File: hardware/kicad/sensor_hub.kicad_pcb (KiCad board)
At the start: 2 copper layers, 0 parts

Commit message: hardware: first board placement, outline and 230 VAC design rules
- Board 100 x 100 mm (fits 8 mm MAINS separation + socketed Pico WH),
  4x M3 holes (board-only), 2 mm isolation slots: under the relays
  (coil | contacts) and along the MAINS zone boundary
- Zone placement: power + ADC + pH top/left (BNC at left edge), Pico WH
  centre (USB at top), relays + W6/W7 + snubbers in MAINS zone top right,
  sensor ports along the bottom edge
- Net classes (Default/Power/VSYS/MAINS) and sensor_hub.kicad_dru:
  MAINS<->SELV 8 mm clearance/creepage/hole clearance, K1<->K2 4 mm
- Rule areas: MAINS (no pour/vias), pH high-Z (no pour), Pico W antenna
- J1 changed to TE 1-1478035-0 (all shield pads = pad 2)
- DRC: 0 clearance/creepage/courtyard errors, schematic parity clean;
  only unrouted nets and silkscreen cosmetics remain

Co-Authored-By: Claude Opus 5.5 <noreply@anthropic.com>
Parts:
- added C1: 100nF, Capacitor_SMD:C_0603_1608Metric, F.Cu at (64.0, 98.5)
- added C10: 100nF, Capacitor_SMD:C_0603_1608Metric, F.Cu at (93.5, 72.0)
- added C11: 100nF, Capacitor_SMD:C_0603_1608Metric, F.Cu at (48.0, 54.0)
- added C12: 100nF, Capacitor_SMD:C_0603_1608Metric, F.Cu at (52.0, 65.0)
- added C13: 10uF, Capacitor_SMD:C_0805_2012Metric, F.Cu at (44.0, 54.0)
- added C14: 10uF, Capacitor_SMD:C_0805_2012Metric, F.Cu at (52.0, 54.0)
- added C15: 10uF, Capacitor_SMD:C_0805_2012Metric, F.Cu at (44.0, 65.0)
- added C16: 10uF, Capacitor_SMD:C_0805_2012Metric, F.Cu at (62.5, 74.0)
- added C17: 1uF, Capacitor_SMD:C_0603_1608Metric, F.Cu at (56.0, 54.0)
- added C18: 1uF, Capacitor_SMD:C_0603_1608Metric, F.Cu at (48.0, 65.0)
- added C19: 100nF X2 275VAC, Capacitor_THT:C_Rect_L13.0mm_W6.0mm_P10.00mm_FKS3_FKP3_MKS4, F.Cu at (112.8, 73.8)
- added C2: 100nF, Capacitor_SMD:C_0603_1608Metric, F.Cu at (65.0, 94.0)
- added C20: 100nF X2 275VAC, Capacitor_THT:C_Rect_L13.0mm_W6.0mm_P10.00mm_FKS3_FKP3_MKS4, F.Cu at (127.1, 83.6)
- added C3: 100nF, Capacitor_SMD:C_0603_1608Metric, F.Cu at (59.5, 112.0)
- added C4: 100nF, Capacitor_SMD:C_0603_1608Metric, F.Cu at (66.5, 112.0)
- added C5: 100nF, Capacitor_SMD:C_0603_1608Metric, F.Cu at (70.0, 112.0)
- added C6: 100nF, Capacitor_SMD:C_0603_1608Metric, F.Cu at (52.5, 112.0)
- added C7: 100nF, Capacitor_SMD:C_0603_1608Metric, F.Cu at (58.5, 74.0)
- added C8: 100nF, Capacitor_SMD:C_0603_1608Metric, F.Cu at (60.0, 54.0)
- added C9: 100nF, Capacitor_SMD:C_0603_1608Metric, F.Cu at (61.5, 68.5)
- added D1: BAV99, Package_TO_SOT_SMD:SOT-23, F.Cu at (59.0, 91.5)
- added D2: 1N4148W, Diode_SMD:D_SOD-123, F.Cu at (98.5, 72.0)
- added D3: 1N4148W, Diode_SMD:D_SOD-123, F.Cu at (98.5, 75.5)
- added H1: MountingHole_3.2mm_M3, MountingHole:MountingHole_3.2mm_M3, F.Cu at (43.5, 43.5)
- added H2: MountingHole_3.2mm_M3, MountingHole:MountingHole_3.2mm_M3, F.Cu at (43.5, 136.5)
- added H3: MountingHole_3.2mm_M3, MountingHole:MountingHole_3.2mm_M3, F.Cu at (136.5, 136.5)
- added H4: MountingHole_3.2mm_M3, MountingHole:MountingHole_3.2mm_M3, F.Cu at (136.5, 100.0)
- added HDR1: Debug-UART, Connector_PinHeader_2.54mm:PinHeader_1x04_P2.54mm_Vertical, F.Cu at (94.3, 97.8)
- added J1: 1-1478035-0, Connector_Coaxial:BNC_TEConnectivity_1478035_Horizontal, F.Cu at (47.6, 92.0)
- added J10: Wago-Relay2, TerminalBlock_WAGO:TerminalBlock_WAGO_236-403_1x03_P5.00mm_45Degree, F.Cu at (130.5, 74.8)
- added J11: Spare-GPIO, Connector_PinHeader_2.54mm:PinHeader_2x08_P2.54mm_Vertical, F.Cu at (71.3, 101.9)
- added J2: Wago-DS18B20, TerminalBlock_WAGO:TerminalBlock_WAGO_2601-1103_1x03_P3.50mm_Horizontal, F.Cu at (66.2, 133.9)
- added J3: Wago-DHT22, TerminalBlock_WAGO:TerminalBlock_WAGO_2601-1103_1x03_P3.50mm_Horizontal, F.Cu at (79.9, 133.9)
- added J4: Wago-PIR, TerminalBlock_WAGO:TerminalBlock_WAGO_2601-1103_1x03_P3.50mm_Horizontal, F.Cu at (93.6, 133.9)
- added J5: Wago-GP16, TerminalBlock_WAGO:TerminalBlock_WAGO_2601-1103_1x03_P3.50mm_Horizontal, F.Cu at (107.3, 133.9)
- added J6: Wago-GP17, TerminalBlock_WAGO:TerminalBlock_WAGO_2601-1103_1x03_P3.50mm_Horizontal, F.Cu at (121.0, 133.9)
- added J7: Wago-Relay1, TerminalBlock_WAGO:TerminalBlock_WAGO_236-403_1x03_P5.00mm_45Degree, F.Cu at (130.5, 55.3)
- added J8: Phoenix-EC4pin, TerminalBlock_Phoenix:TerminalBlock_Phoenix_PT-1,5-4-3.5-H_1x04_P3.50mm_Horizontal, F.Cu at (49.8, 134.8)
- added J9: Phoenix-Power, TerminalBlock_Phoenix:TerminalBlock_Phoenix_PT-1,5-2-5.0-H_1x02_P5.00mm_Horizontal, F.Cu at (56.5, 45.8)
- added K1: G2RL-1-E DC5, Relay_THT:Relay_SPDT_Omron_G2RL-1-E, F.Cu at (97.6, 51.3)
- added K2: G2RL-1-E DC5, Relay_THT:Relay_SPDT_Omron_G2RL-1-E, F.Cu at (97.6, 66.3)
- added NT1: NetTie_2, NetTie:NetTie-2_SMD_Pad0.5mm, F.Cu at (52.0, 78.5)
- added Q1: BC817-40, Package_TO_SOT_SMD:SOT-23, F.Cu at (94.0, 79.5)
- added Q2: BSS84PXUMA1, Package_TO_SOT_SMD:SOT-23, F.Cu at (101.0, 118.0)
- added Q3: BC817-40, Package_TO_SOT_SMD:SOT-23, F.Cu at (94.0, 85.0)
- added R1: 10M, Resistor_SMD:R_0603_1608Metric, F.Cu at (59.0, 87.0)
- added R10: 4k7, Resistor_SMD:R_0603_1608Metric, F.Cu at (63.0, 45.0)
- added R11: 4k7, Resistor_SMD:R_0603_1608Metric, F.Cu at (66.0, 45.0)
- added R15: 10k, Resistor_SMD:R_0603_1608Metric, F.Cu at (56.0, 112.0)
- added R16: 10k, Resistor_SMD:R_0603_1608Metric, F.Cu at (63.0, 112.0)
- added R17: 10k, Resistor_SMD:R_0603_1608Metric, F.Cu at (101.0, 114.0)
- added R18: 1k, Resistor_SMD:R_0603_1608Metric, F.Cu at (99.5, 85.0)
- added R19: 100R, Resistor_SMD:R_1206_3216Metric, F.Cu at (109.5, 74.0)
- added R2: 100k, Resistor_SMD:R_0603_1608Metric, F.Cu at (57.0, 97.0)
- added R20: 100R, Resistor_SMD:R_1206_3216Metric, F.Cu at (123.2, 83.7)
- added R3: 100k, Resistor_SMD:R_0603_1608Metric, F.Cu at (60.5, 97.0)
- added R5: 4k7, Resistor_SMD:R_0603_1608Metric, F.Cu at (70.0, 120.5)
- added R6: 10k, Resistor_SMD:R_0603_1608Metric, F.Cu at (83.5, 120.5)
- added R7: 10k, Resistor_SMD:R_0603_1608Metric, F.Cu at (49.0, 112.0)
- added R8: 1k, Resistor_SMD:R_0603_1608Metric, F.Cu at (99.5, 79.5)
- added R9: 10k, Resistor_SMD:R_0603_1608Metric, F.Cu at (95.0, 120.5)
- added U1: Pico WH, Module:RaspberryPi_Pico_Common_THT, F.Cu at (71.0, 44.0)
- added U2: ADS1115IDGSR, Package_SO:MSOP-10_3x3mm_P0.5mm, F.Cu at (52.0, 74.0)
- added U4: AD8603ARTZ-R2, Package_TO_SOT_SMD:TSOT-23-5, F.Cu at (64.5, 89.0)
- added U5: AP2112K-3.3TRG1, Package_TO_SOT_SMD:SOT-23-5, F.Cu at (52.0, 59.5)
- added U6: VEML7700-TT, sensor_hub:VEML7700_TT, F.Cu at (61.5, 65.4)
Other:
- board outline added: 100 x 100 mm
- board text added: "! 230 VAC max 5 A - MAINS"
- board text added: "5V IN"
- board text added: "EC W Y R B"
- board text added: "PH"
- board text added: "Sensor Hub V2.0 2026-09"
- board text added: "W1 DS18B20"
- board text added: "W2 DHT22"
- board text added: "W3 PIR"
- board text added: "W4 GP16"
- board text added: "W5 GP17"
- board text added: "W6 RELAY1"
- board text added: "W7 RELAY2"

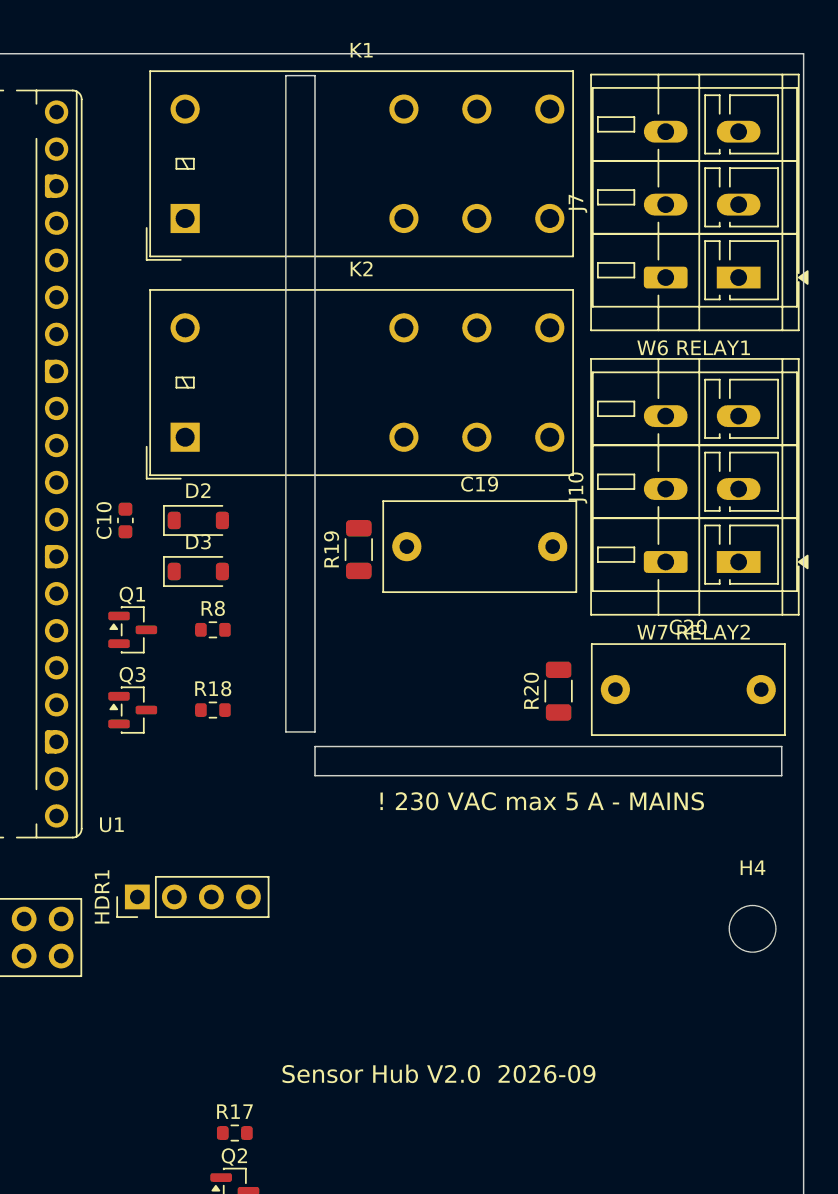
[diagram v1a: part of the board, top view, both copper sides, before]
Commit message: hardware: upright relays with terminals aligned to contact rows, remap W6/W7 pins
Co-Authored-By: Claude Opus 5.5 <noreply@anthropic.com>
Claude-Session: https://claude.ai/code/session_01PDHupfXBxwLmo1MxXKJEdB
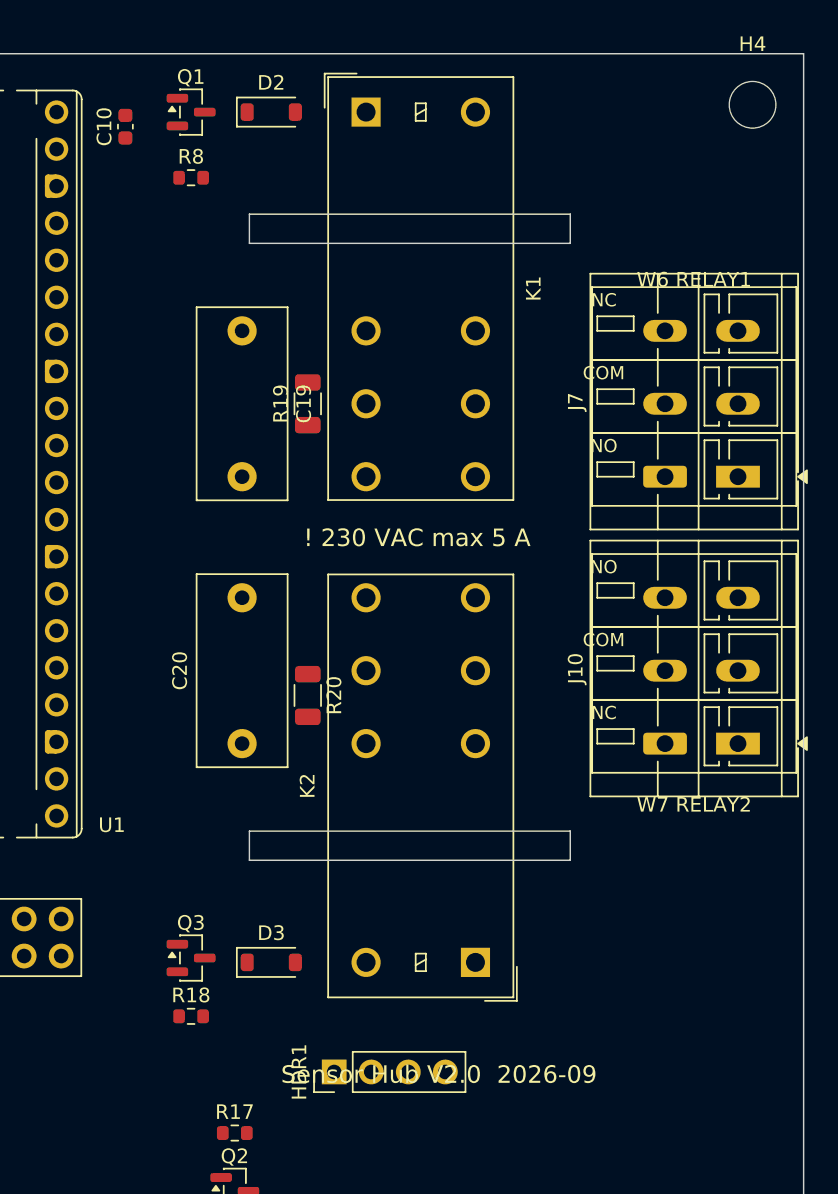
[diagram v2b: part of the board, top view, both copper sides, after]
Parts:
- moved H4 56.5 mm to (136.5, 43.5)
- moved K2 41.1 mm to (117.5, 102.3), turned to 180 degrees
- moved Q1 35.7 mm to (98.0, 44.0)
- moved R8 31.0 mm to (98.0, 48.5)
- moved D2 28.4 mm to (103.5, 44.0)
- moved D3 27.3 mm to (103.5, 102.3)
- moved C10 27.0 mm to (93.5, 45.0)
- moved C20 25.9 mm to (101.5, 87.3), turned to 90 degrees
- moved R18 21.1 mm to (98.0, 106.0)
- moved C19 18.6 mm to (101.5, 59.0), turned to -90 degrees
- moved HDR1 18.1 mm to (107.8, 109.8)
- moved Q3 17.5 mm to (98.0, 102.0)
- moved R20 17.2 mm to (106.0, 84.0), turned to -90 degrees
- moved K1 14.4 mm to (110.0, 44.0), turned to 0 degrees
- moved J7 13.7 mm to (130.5, 69.0)
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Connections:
- J10 pad 1: /K2_COM -> /K2_NC
- J10 pad 2: /K2_NO -> /K2_COM
- J10 pad 3: /K2_NC -> /K2_NO
- J7 pad 1: /K1_COM -> /K1_NO
- J7 pad 2: /K1_NO -> /K1_COM
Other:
- outline, holes or cut-outs redrawn
- board text added: "! 230 VAC max 5 A"
- board text added: "COM"
- board text added: "NC"
- board text added: "NO"
- board text removed: "! 230 VAC max 5 A - MAINS"

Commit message: hardware: route board (mains + NODE_A by hand, rest Freerouting), GND/GND_ANA/guard pours
Antenna keepout narrowed to the area between the Pico pin rows; it covered
pins 15-26 and made them unroutable. Still open: J11 GP20/21/22/26,
3V3_ANA at U2, 5 dangling vias, B.Cu guard not stitched.

Co-Authored-By: Claude Opus 5.5 <noreply@anthropic.com>
Claude-Session: https://claude.ai/code/session_01PDHupfXBxwLmo1MxXKJEdB
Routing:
- net /GND: track 0.00 -> 392.1 mm, vias 0 -> 2
- net /3V3_DIG: track 0.00 -> 288.7 mm, vias 0 -> 3
- net /VSYS: track 0.00 -> 251.4 mm, vias 0 -> 6
- net /GND_ANA: track 0.00 -> 164.6 mm, vias 0 -> 2
- net /3V3_ANA: track 0.00 -> 105.6 mm, vias 0 -> 5
- net /DHT_DATA: track 0.00 -> 101.0 mm, vias 0 -> 1
- net /UART_RX: track 0.00 -> 92.3 mm, vias 0 -> 1
- net /PIR_OUT: track 0.00 -> 91.4 mm, vias 0 -> 1
- net /UART_TX: track 0.00 -> 91.0 mm
- net /GP28: track 0.00 -> 85.2 mm, vias 0 -> 1
- net /ONEWIRE: track 0.00 -> 74.6 mm, vias 0 -> 2
- net /W5_SIG: track 0.00 -> 73.0 mm
- net /NODE_NTC: track 0.00 -> 67.1 mm, vias 0 -> 2
- net /PIR_EN_N: track 0.00 -> 63.5 mm, vias 0 -> 2
- net /GP27: track 0.00 -> 57.7 mm, vias 0 -> 1
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- added copper zone on B.Cu, net /GND
- added copper zone on F.Cu, net /GND
- added copper zone on B.Cu, net /GND_ANA
- added copper zone on F.Cu, net /GND_ANA
- added copper zone on B.Cu, net /PH_BUF
- added copper zone on F.Cu, net /PH_BUF

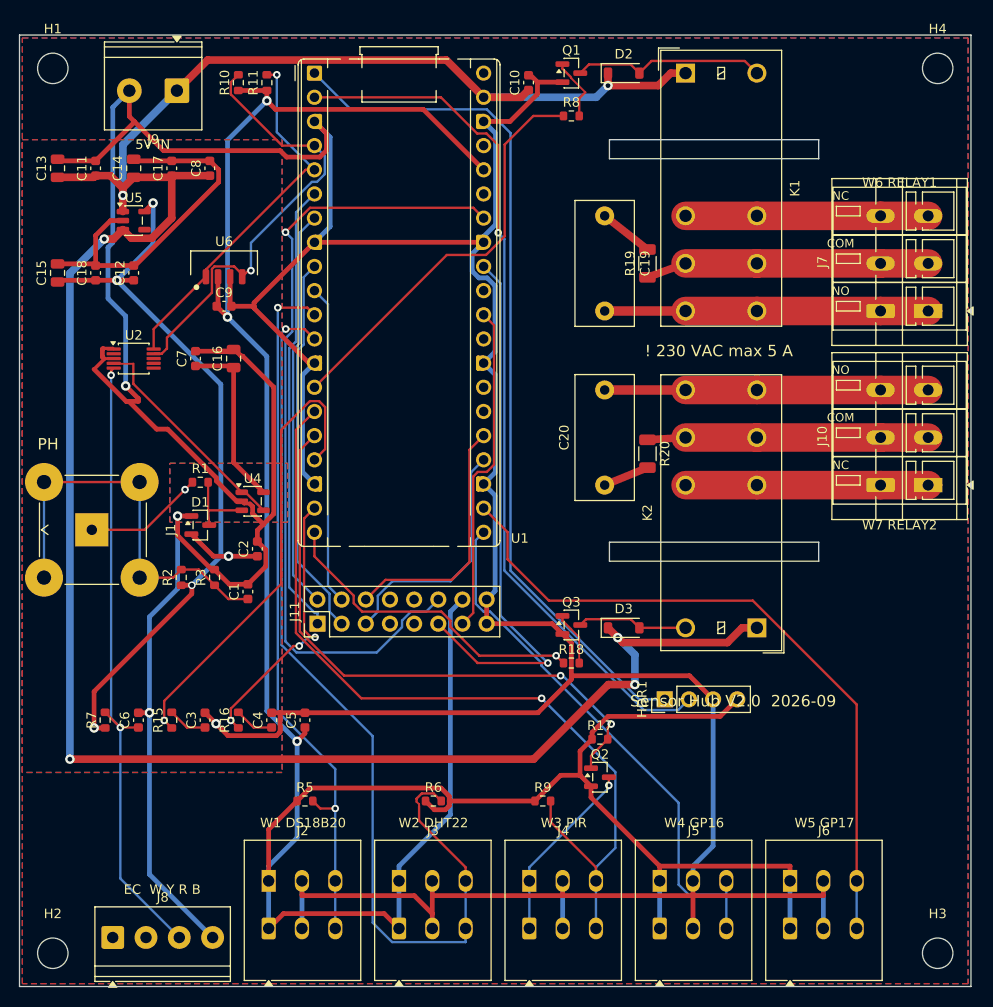
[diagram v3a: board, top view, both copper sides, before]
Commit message: hardware: complete routing, copper DRC clean
- 3V3_ANA pre-routed off U2 pin 8 (0.5 mm pitch too tight for Power width)
- J11 spare GPIOs pre-routed down the gap between antenna keepout and pin row
- B.Cu guard pour stitched to PH_BUF next to U4
- dangling vias/stubs stripped after Freerouting
- place_pcb: antenna keepout only between the Pico pin rows
- DRC: header/socket GND pins may use one thermal spoke per layer
- route_pcb/autoroute: Delete instead of Remove (segfault), fail loudly

Co-Authored-By: Claude Opus 5.5 <noreply@anthropic.com>
Claude-Session: https://claude.ai/code/session_01PDHupfXBxwLmo1MxXKJEdB
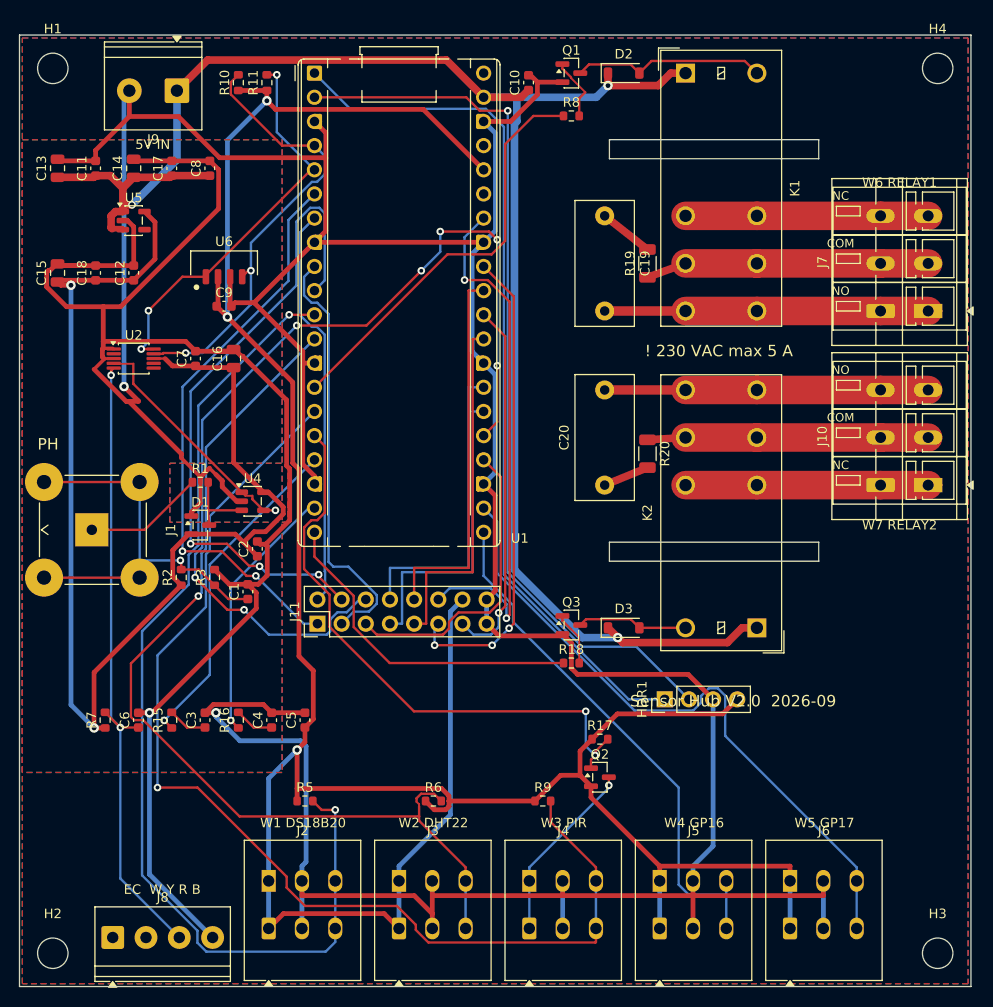
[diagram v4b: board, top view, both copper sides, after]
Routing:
- net /GP19: track 26.4 -> 101.5 mm, vias 0 -> 7
- net /VSYS: track 251.4 -> 182.8 mm, vias 6 -> 3
- net /GP26: track 0.00 -> 39.8 mm
- net /GP22: track 0.00 -> 37.2 mm
- net /GP7: track 33.6 -> 69.3 mm, vias 0 -> 3
- net /ONEWIRE: track 74.6 -> 109.4 mm
- net /GP21: track 0.00 -> 32.2 mm
- net /GP20: track 0.00 -> 32.1 mm
- net /GP28: track 85.2 -> 56.3 mm, vias 1 -> 2
- net /3V3_ANA: track 105.6 -> 132.4 mm, vias 5 -> 2
- net /PIR_OUT: track 91.4 -> 117.0 mm
- net /GND_ANA: track 164.6 -> 188.9 mm, vias 2 -> 1
- net /EC_PWM_A: track 48.9 -> 35.1 mm
- net /GND: track 392.1 -> 378.5 mm
- net /GP4: track 47.7 -> 60.6 mm, vias 0 -> 2
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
